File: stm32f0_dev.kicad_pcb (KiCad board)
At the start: 2 copper layers, 21.5 x 48.2 mm, 29 parts, among them J1 USB_C_Receptacle_USB2.0, J2 pins_left, J4 pins_right, SW1 SW_Push, SW2 SW_SPDT, U1 STM32F030K6Tx, U2 AP2112K-3.3, U3 SN74LVC2G04DCKR, U4 CH340C, U5 MT29F2G01ABAGDWB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

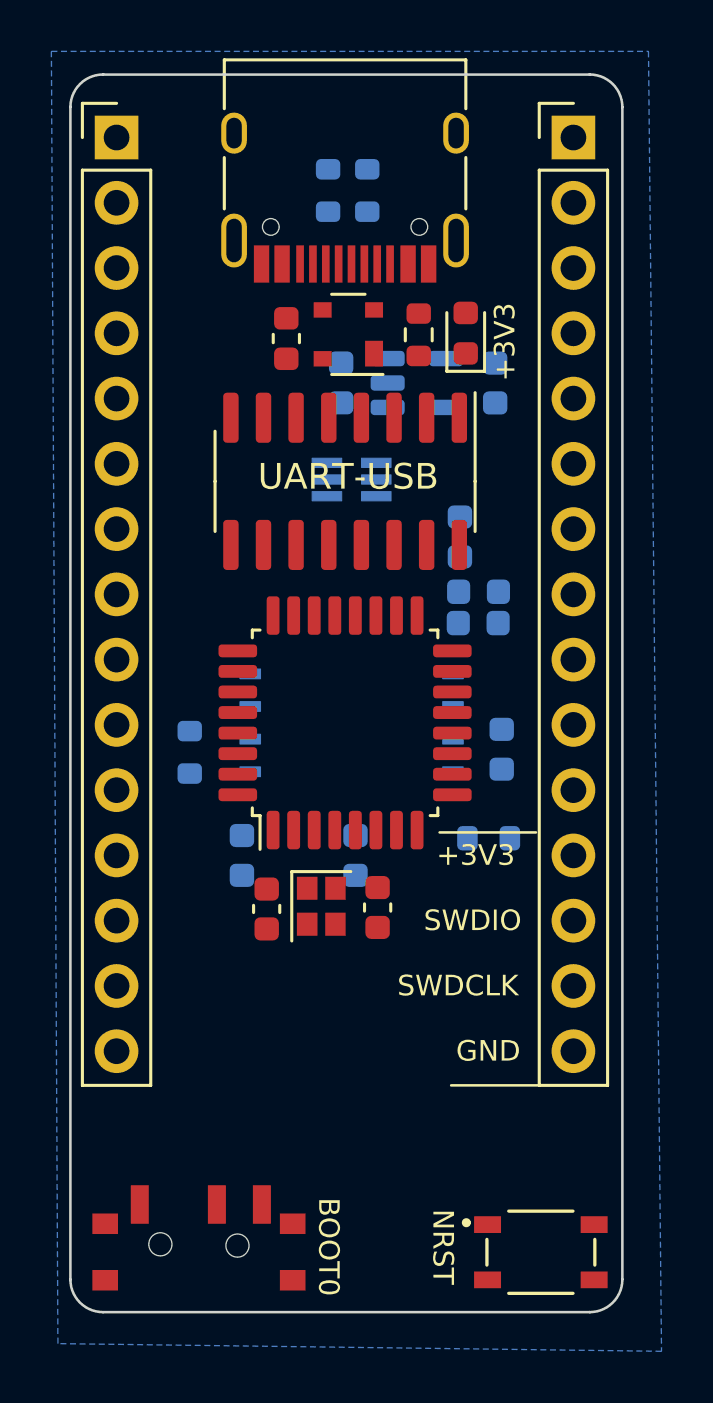
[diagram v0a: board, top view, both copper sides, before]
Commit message: Schematic done, routing done, to fix issues on board
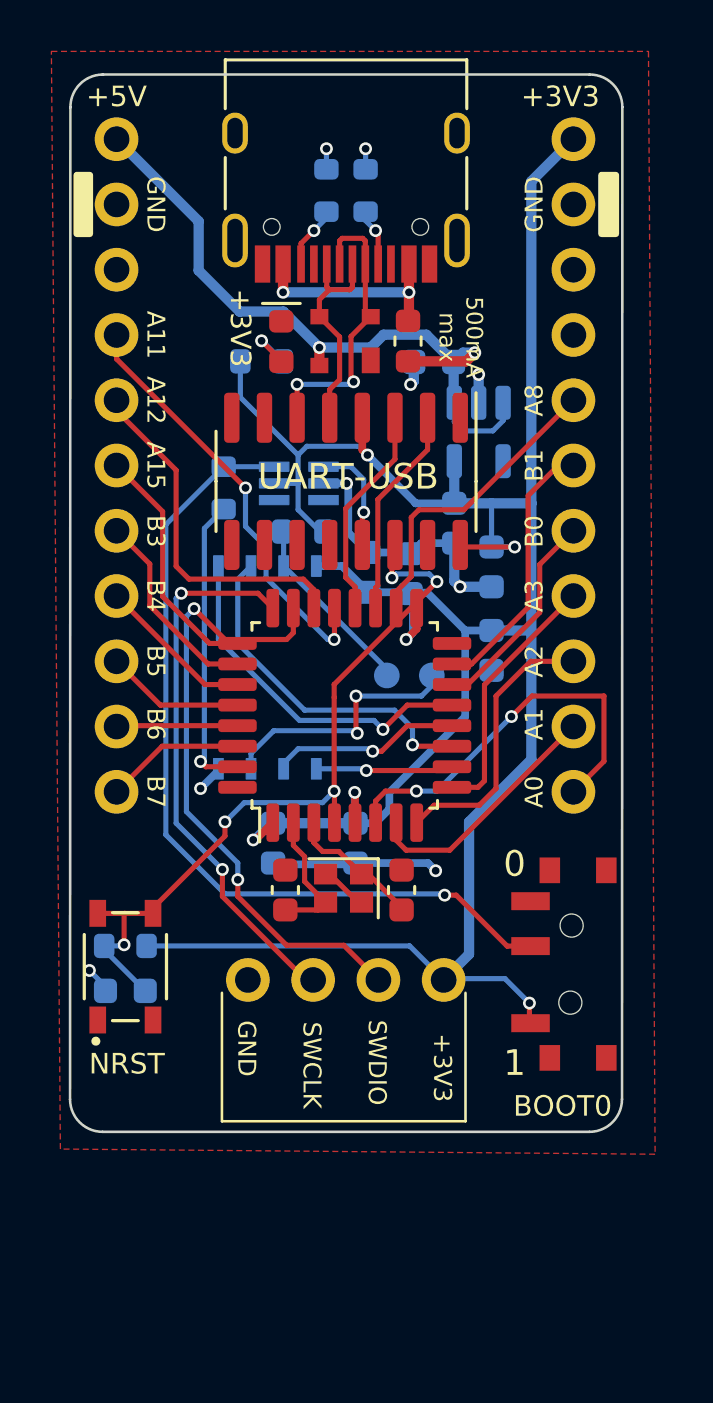
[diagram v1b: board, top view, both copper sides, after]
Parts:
- added C11: 1u, Capacitor_SMD:C_0603_1608Metric, B.Cu at (145.9, 125.2)
- added J3: SWD_header, Connector_PinHeader_2.54mm:PinHeader_1x04_P2.54mm_Vertical, F.Cu at (158.3, 124.8)
- added R6: 22k, Resistor_SMD:R_0603_1608Metric, B.Cu at (145.9, 123.5)
- added TP1: TestPoint, TestPoint:TestPoint_Pad_D1.0mm, B.Cu at (156.1, 112.9)
- added TP2: TestPoint, TestPoint:TestPoint_Pad_D1.0mm, B.Cu at (157.8, 112.9)
- J2: value pins_left -> left_bank; footprint Connector_PinHeader_2.54mm:PinHeader_1x15_P2.54mm_Vertical -> Connector_PinHeader_2.54mm:PinHeader_1x11_P2.54mm_Vertical
- J4: value pins_right -> right_bank; footprint Connector_PinHeader_2.54mm:PinHeader_1x15_P2.54mm_Vertical -> Connector_PinHeader_2.54mm:PinHeader_1x11_P2.54mm_Vertical
- R1: moved to B.Cu
- moved SW1 19.6 mm to (145.9, 124.3), turned to 90 degrees
- moved SW2 18.2 mm to (163.3, 124.1), turned to 90 degrees
- moved R5 13.9 mm to (152.8, 107.3)
- moved R4 10.4 mm to (149.7, 105.6)
- moved C6 8.63 mm to (155.3, 108.9), turned to 90 degrees
- moved D1 7.18 mm to (152.0, 99.9), turned to -90 degrees
- moved R1 6.20 mm to (151.2, 100.7), turned to 0 degrees
- moved C5 5.68 mm to (158.7, 107.0), turned to -90 degrees
- moved F1 4.74 mm to (156.9, 99.9)
- moved U5 3.92 mm to (151.4, 112.6), turned to 90 degrees
- moved C4 3.69 mm to (157.9, 100.7), turned to 180 degrees
- moved C10 3.26 mm to (157.0, 109.0), turned to 90 degrees
- moved U2 3.07 mm to (159.6, 103.5), turned to -90 degrees
- moved C7 2.34 mm to (160.1, 112.0), turned to -90 degrees
- moved U3 2.06 mm to (152.6, 105.5), turned to 180 degrees
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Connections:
- C2 pad 2: Net-(C2-Pad2) -> GND
- C3 pad 2: Net-(C2-Pad2) -> GND
- U1 pad 10: /NSS -> /NAND_CS
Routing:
- net +3V3: track 0.00 -> 108.6 mm, vias 0 -> 6
- net /BOOT0: track 0.00 -> 33.2 mm, vias 0 -> 1
- net /NRST: track 0.00 -> 30.4 mm, vias 0 -> 5
- net +5V: track 0.00 -> 27.9 mm, vias 0 -> 2
- net GND: track 0.00 -> 24.6 mm, vias 0 -> 9
- net /PA13/SWDIO: track 0.00 -> 24.4 mm, vias 0 -> 2
- net /PA14/SWDCLK: track 0.00 -> 21.3 mm, vias 0 -> 2
- net /PA11: track 0.00 -> 16.7 mm, vias 0 -> 2
- net /PA0: track 0.00 -> 15.6 mm, vias 0 -> 2
- net /PA12: track 0.00 -> 13.9 mm
- net /MOSI: track 0.00 -> 13.8 mm, vias 0 -> 1
- net /SCK: track 0.00 -> 13.6 mm, vias 0 -> 1
- net /PA8: track 0.00 -> 12.0 mm
- net Net-(R4-Pad2): track 0.00 -> 11.7 mm, vias 0 -> 1
- net /D-: track 0.00 -> 11.5 mm, vias 0 -> 2
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- added copper zone on F.Cu, net GND
- removed copper zone on B.Cu, net GND
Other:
- board size 21.5 x 48.2 mm -> 21.5 x 41.2 mm
- board text added: "+5V"
- board text added: "0"
- board text added: "1"
- board text added: "500mA max"
- board text added: "A0"
- board text added: "A1"
- board text added: "A11"
- board text added: "A12"
- board text added: "A15"
- board text added: "A2"
- board text added: "A3"
- board text added: "A8"
- board text added: "B0"
- board text added: "B1"
- board text added: "B3"
- board text added: "B4"
- board text added: "B5"
- board text added: "B6"
- board text added: "B7"
- board text added: "SWCLK"
- board text removed: "SWDCLK"

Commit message: Finished board, added gerber folder, uart leds, board dimensions
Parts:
- added D3: RED, LED_SMD:LED_0603_1608Metric, F.Cu at (160.5, 99.9)
- added D4: RED, LED_SMD:LED_0603_1608Metric, F.Cu at (148.7, 99.9)
- added R7: 3k3, Resistor_SMD:R_0603_1608Metric, B.Cu at (160.5, 99.9)
- added R8: 3k3, Resistor_SMD:R_0603_1608Metric, B.Cu at (148.7, 99.9)
- TP1: value TestPoint -> HOLD
- TP2: value TestPoint -> WP
- moved SW2 0.57 mm to (162.7, 124.1)
- moved J3 0.49 mm to (158.3, 124.3)
- moved C11 0.44 mm to (146.3, 125.2)
- moved R6 0.44 mm to (146.3, 123.5)
- moved SW1 0.44 mm to (146.3, 124.3)
- moved TP1 0.20 mm to (155.9, 112.9)
- moved U3 0.13 mm to (152.6, 105.3)
- moved J2 0.08 mm to (145.6, 92.1)
- turned D1 to 90 degrees
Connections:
- U4 pad 2: /TX -> /RX
- U4 pad 3: /RX -> /TX
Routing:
- net /RX: track 8.35 -> 19.7 mm, vias 0 -> 2
- net /NRST: track 30.4 -> 39.8 mm
- net /PA0: track 15.6 -> 9.96 mm
- net /TX: track 8.25 -> 13.7 mm
- net +3V3: track 108.6 -> 112.8 mm
- net Net-(D3-Pad2): track 0.00 -> 1.95 mm, vias 0 -> 1
- net Net-(D4-Pad2): track 0.00 -> 1.73 mm, vias 0 -> 1
- net /SCK: track 13.6 -> 11.9 mm
- net /PA13/SWDIO: track 24.4 -> 23.2 mm
- net GND: track 24.6 -> 25.7 mm, vias 9 -> 10
- net /MOSI: track 13.8 -> 12.9 mm
- net /PA1: track 9.74 -> 10.6 mm, vias 0 -> 1
- net /PA12: track 13.9 -> 13.2 mm
- net /PA14/SWDCLK: track 21.3 -> 20.7 mm
- net /PA11: track 16.7 -> 17.3 mm
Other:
- board size 21.5 x 41.2 mm -> 20.4 x 40.6 mm
- board text added: "500mA"
- board text added: "JLCJLCJLCJLC"
- board text added: "MT29F2G0 1ABAGDWB"
- board text added: "RX"
- board text added: "TX"
- board text removed: "500mA max"

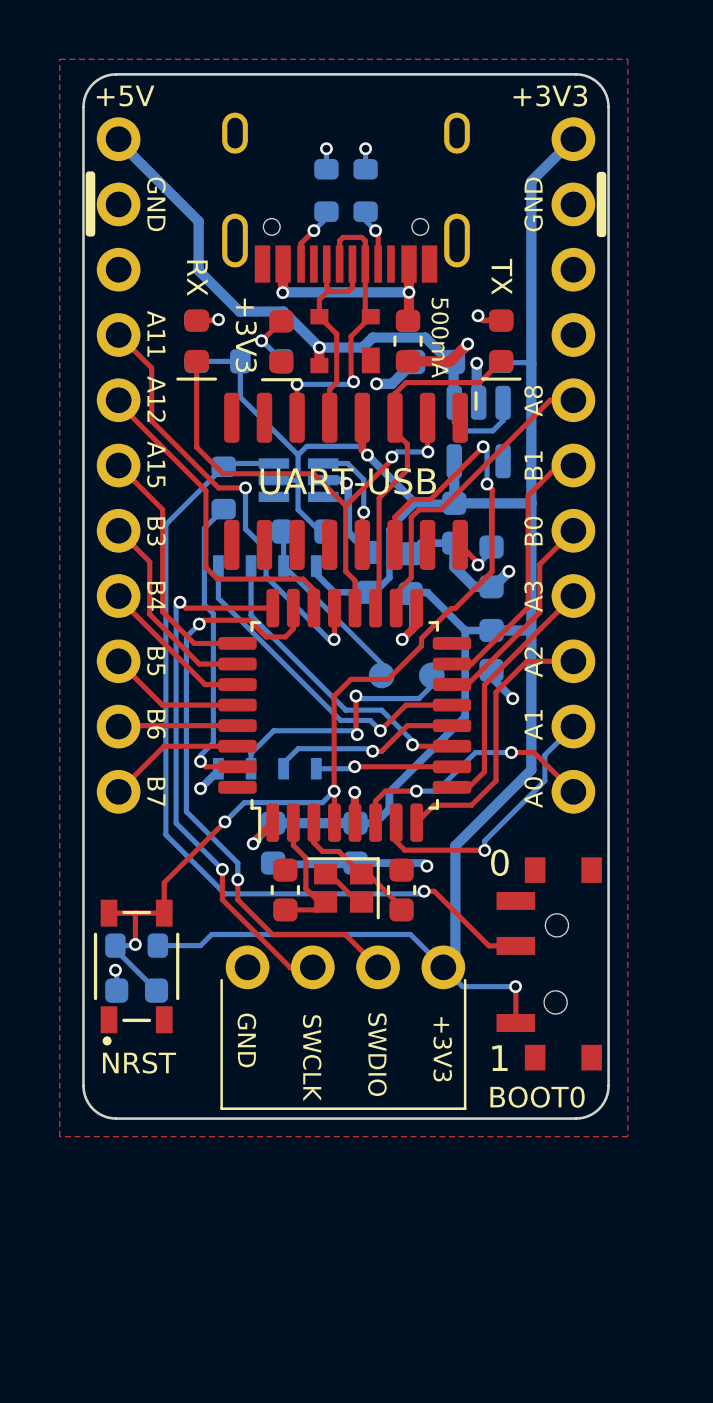
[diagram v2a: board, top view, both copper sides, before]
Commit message: Fixed nrst button, dtr signal
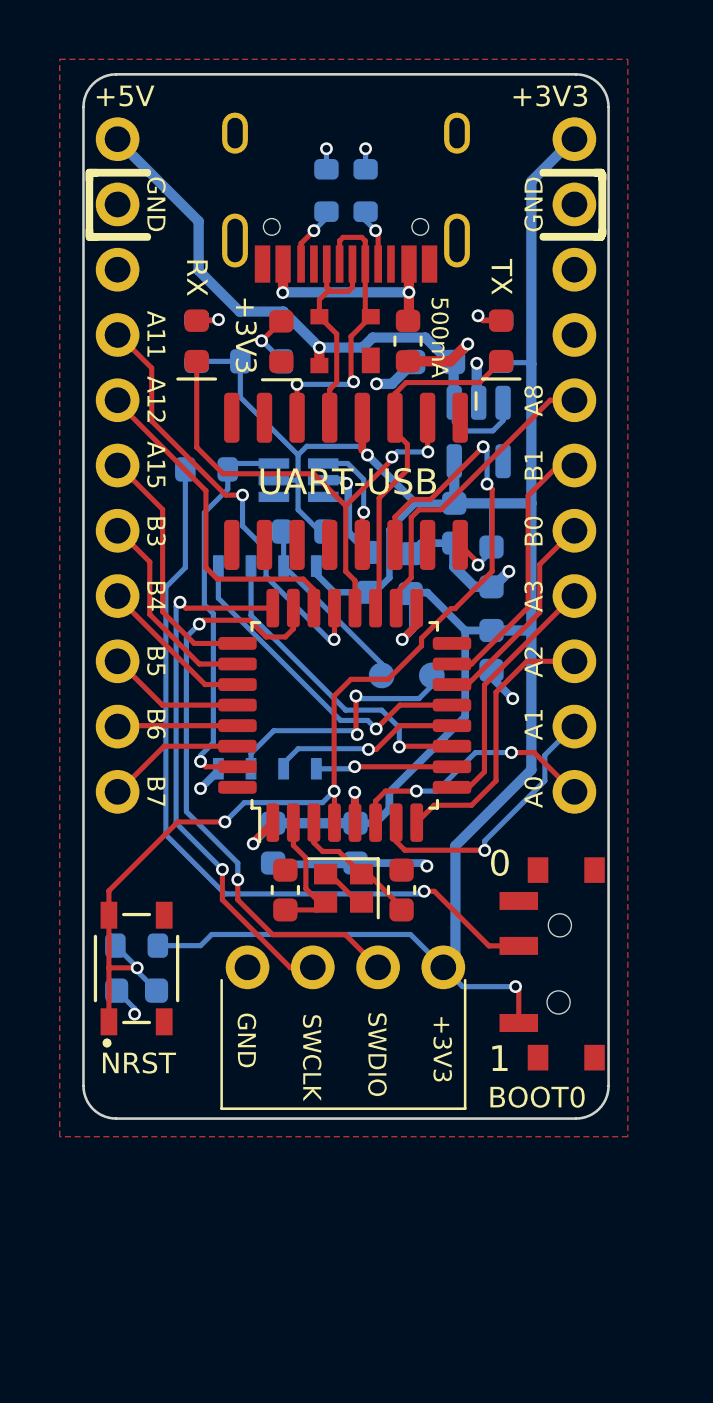
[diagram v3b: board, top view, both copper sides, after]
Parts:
- SW1: value SW_Push -> SW_Push_Open_Dual
- TP1: value HOLD -> TestPoint
- TP2: value WP -> TestPoint
- moved R4 0.98 mm to (149.0, 104.9), turned to 0 degrees
- moved SW2 0.11 mm to (162.8, 124.1)
- moved SW1 0.08 mm to (146.3, 124.3)
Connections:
- R4 pad 1: /BOOT0 -> Net-(R4-Pad1)
- R4 pad 2: Net-(R4-Pad2) -> /BOOT0
- SW1 pad 1: GND -> /NRST
- SW2 pad 2: /BOOT0 -> Net-(R4-Pad1)
- U1 pad 31: Net-(R4-Pad2) -> /BOOT0
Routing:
- net Net-(R4-Pad1): track 0.00 -> 30.1 mm, vias 0 -> 1
- net /BOOT0: track 32.8 -> 15.5 mm
- net Net-(R4-Pad2): track 12.0 -> 0.00 mm, vias 1 -> 0
- net /NRST: track 39.8 -> 43.0 mm
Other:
- board text added: "STM32F0 breakout Stefano Nicolis September 2022-REV 1"
- board text removed: "STM32F0 breakout Stefano Nicolis September 2022"

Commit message: Removed useless boot0 switch, uart IC is driving that signal
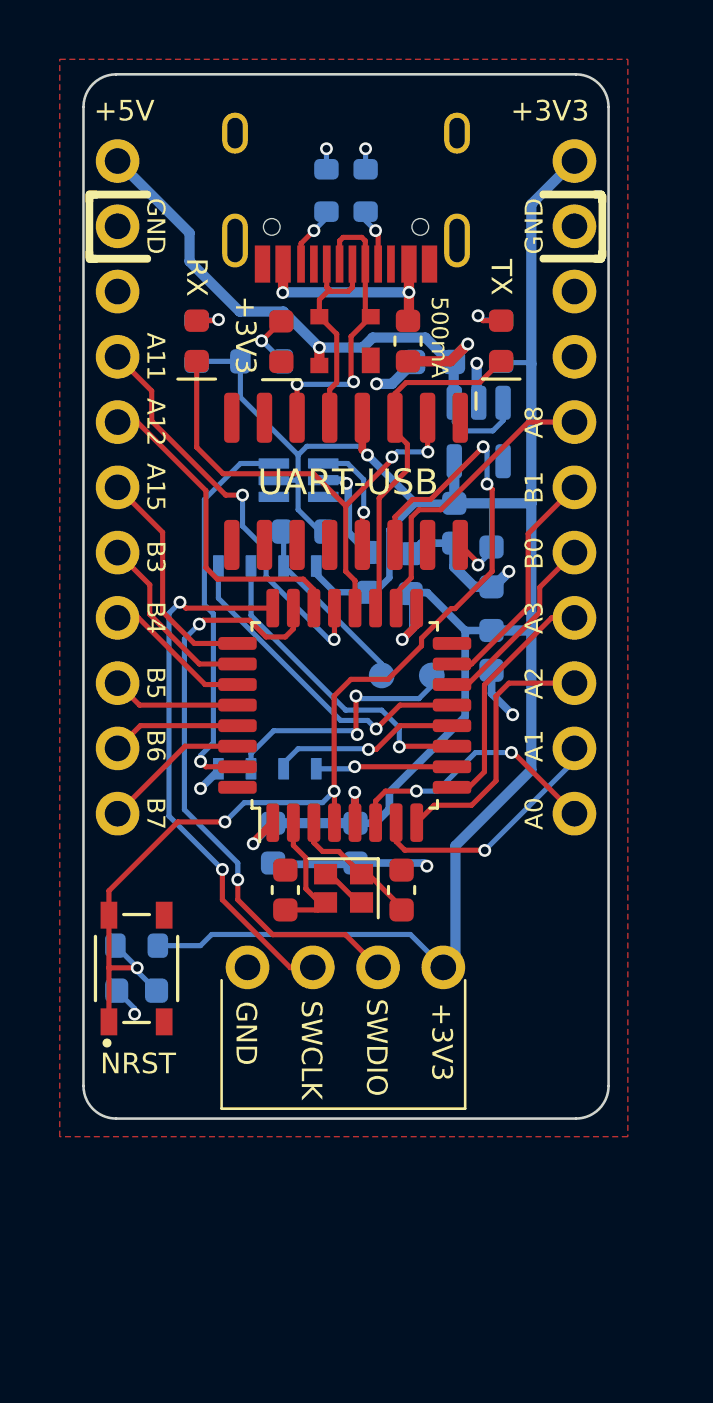
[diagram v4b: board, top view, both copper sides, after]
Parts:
- removed R4: 10k, Resistor_SMD:R_0603_1608Metric
- removed SW2: SW_SPDT, SSSS811101 :SSSS811101
- U1: value STM32F030K6Tx -> STM32F030K6T6
- moved J2 0.85 mm to (145.6, 92.9)
- moved J4 0.85 mm to (163.4, 92.9)
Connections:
- net Net-(U3-Pad1) renamed /~{BOOT0}
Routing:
- net Net-(R4-Pad1): track 30.1 -> 0.00 mm, vias 1 -> 0
- net +3V3: track 112.9 -> 107.5 mm, vias 6 -> 5
- net /PB1: track 10.5 -> 9.29 mm
- net +5V: track 27.6 -> 26.8 mm
- net /PB3: track 7.97 -> 7.14 mm
- net /PA15: track 9.83 -> 8.99 mm
- net /PA11: track 17.1 -> 16.2 mm
- net /PB0: track 8.30 -> 7.47 mm
- net /PA1: track 10.6 -> 9.74 mm
- net GND: track 26.1 -> 26.7 mm
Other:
- board text removed: "0"
- board text removed: "1"
- board text removed: "BOOT0"
